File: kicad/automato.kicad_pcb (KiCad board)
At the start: 2 copper layers, 106 x 64 mm, 98 parts, among them J1 USB_C_Receptacle, J2 LiPo, J3 Conn_01x07_Male, J4 Screw_Terminal_01x20, J5 USB_C_Receptacle, J8 Micro_SD_Card_Det, M1 eink-module, Q1 Q_NPN_BCE, Q2 Q_NPN_BCE, Q3 DMG3415U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

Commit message: more routing
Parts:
- moved R17 12.1 mm to (84.6, 71.5)
- moved G*** 11.6 mm to (73.5, 77.0)
- moved C10 11.1 mm to (100.5, 83.9), turned to 180 degrees
- moved R6 10.2 mm to (174.0, 66.8), turned to 270 degrees
- moved R1 9.96 mm to (84.6, 75.6), turned to 0 degrees
- moved R3 9.92 mm to (86.6, 80.7), turned to 90 degrees
- moved C1 8.35 mm to (87.5, 73.7)
- moved C2 8.35 mm to (90.0, 73.7)
- moved R2 8.24 mm to (84.6, 77.8), turned to 180 degrees
- moved C7 8.08 mm to (89.6, 83.1), turned to 180 degrees
- moved D5 7.90 mm to (84.6, 73.5), turned to 0 degrees
- moved JP1 7.21 mm to (169.4, 104.2), turned to 0 degrees
- moved Q1 6.26 mm to (96.8, 83.2), turned to 90 degrees
- moved R5 5.42 mm to (95.2, 76.0), turned to 180 degrees
- moved R4 5.34 mm to (93.5, 83.2), turned to 90 degrees
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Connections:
- J4 pad 10: IO33 -> IO16
- J4 pad 11: IO32 -> 3V3
- J4 pad 12: IO27 -> IO15
- J4 pad 13: IO26 -> GND
- J4 pad 14: VBUS -> IO14
- J4 pad 15: 3V3 -> VBUS
- J4 pad 16: 3V3 -> IO13
- J4 pad 5: GND -> A7
- J4 pad 6: A7 -> A6
- J4 pad 7: A6 -> A1
- J4 pad 8: A1 -> A0
- J4 pad 9: A0 -> 3V3
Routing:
- net VBUS: track 0.00 -> 90.8 mm, vias 0 -> 4
- net EN: track 0.00 -> 80.4 mm, vias 0 -> 4
- net RX: track 0.00 -> 41.6 mm, vias 0 -> 2
- net TX: track 0.00 -> 40.6 mm, vias 0 -> 2
- net RST_LORA: track 0.00 -> 35.4 mm
- net IRQ_LORA: track 0.00 -> 28.5 mm
- net VIN: track 0.00 -> 28.4 mm
- net SPI_CLK: track 0.00 -> 26.5 mm
- net SPI_MISO: track 0.00 -> 26.4 mm
- net CS_LORA: track 0.00 -> 26.3 mm
- net VBAT: track 0.00 -> 26.0 mm, vias 0 -> 2
- net Net-(C3-Pad1): track 0.00 -> 24.6 mm
- net Net-(J3-Pad2): track 0.00 -> 24.1 mm, vias 0 -> 1
- net SPI_MOSI: track 0.00 -> 23.4 mm
- net A0: track 0.00 -> 23.2 mm
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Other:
- net class Default: via_dia 0.8 -> 0.7; via_drill 0.4 -> 0.3

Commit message: add sma
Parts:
- moved TP1 35.4 mm to (153.6, 44.0)
- moved TP2 35.4 mm to (153.6, 47.0)
- moved TP3 35.4 mm to (153.6, 50.0)
- moved TP4 35.4 mm to (153.6, 53.0)
- moved R6 0.73 mm to (173.4, 67.2)
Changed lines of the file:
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@@
   )
   (module Resistor_SMD:R_0805_2012Metric (layer F.Cu)
-    (at 174 66.8 270)
+    (at 173.4 67.2125 270)
     (descr "Resistor SMD 0805 (2012 Metric), square (rectangular) end terminal, IPC_7351 nominal, (Body size source: IPC-SM-782 page 72, https://www.pcb-3d.com/wordpress/wp-content/uploads/ipc-sm-782a_amendment_1_and_2.pdf), generated with kicad-footprint-generator")
     (tags resistor)
@@
   )
   (module TestPoint:TestPoint_Pad_D2.0mm (layer F.Cu)
-    (at 180.25 67.25)
+    (at 153.55 43.95)
     (descr "SMD pad as test Point, diameter 2.0mm")
     (tags "test point SMD pad")
@@
   )
   (module TestPoint:TestPoint_Pad_D2.0mm (layer F.Cu)
-    (at 180.25 70.25)
+    (at 153.55 46.95)
     (descr "SMD pad as test Point, diameter 2.0mm")
     (tags "test point SMD pad")
@@
   )
   (module TestPoint:TestPoint_Pad_D2.0mm (layer F.Cu)
-    (at 180.25 73.25)
+    (at 153.55 49.95)
     (descr "SMD pad as test Point, diameter 2.0mm")
     (tags "test point SMD pad")
@@
   )
   (module TestPoint:TestPoint_Pad_D2.0mm (layer F.Cu)
-    (at 180.25 76.25)
+    (at 153.55 52.95)
     (descr "SMD pad as test Point, diameter 2.0mm")
     (tags "test point SMD pad")

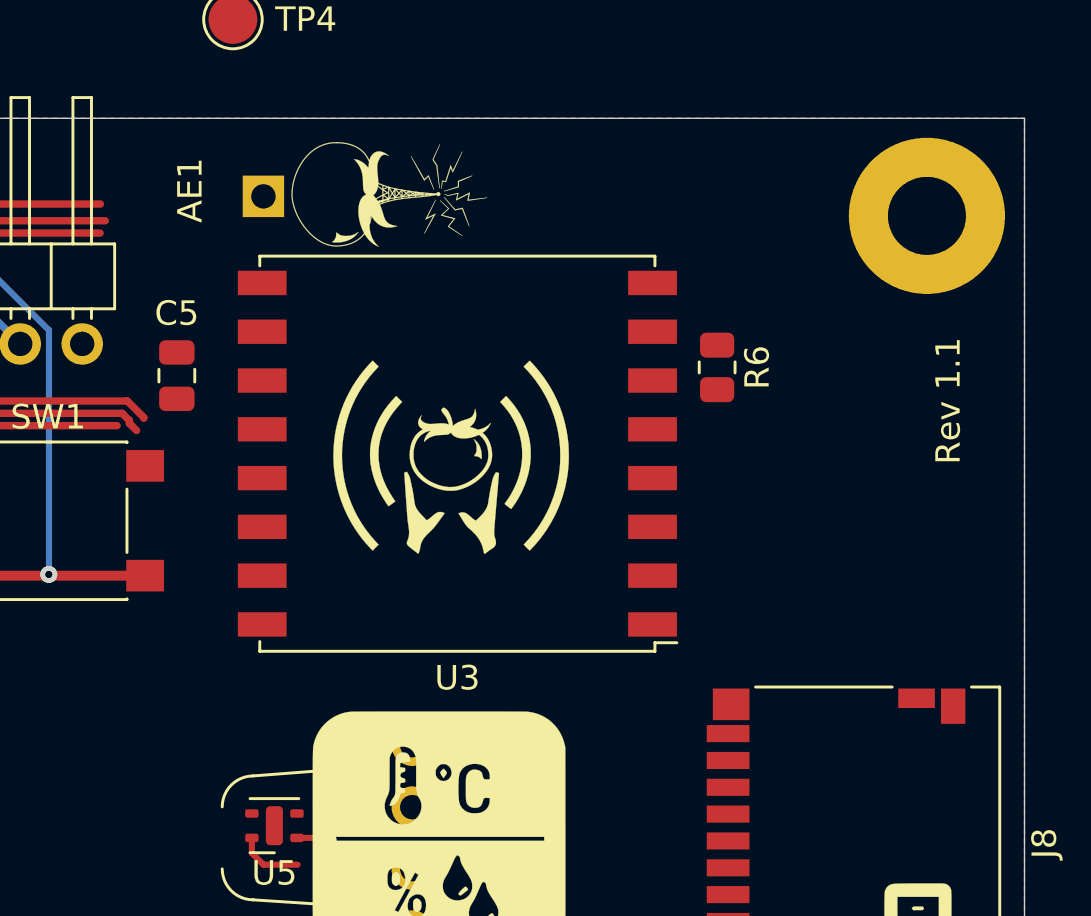
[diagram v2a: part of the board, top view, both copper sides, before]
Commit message: reposition lora
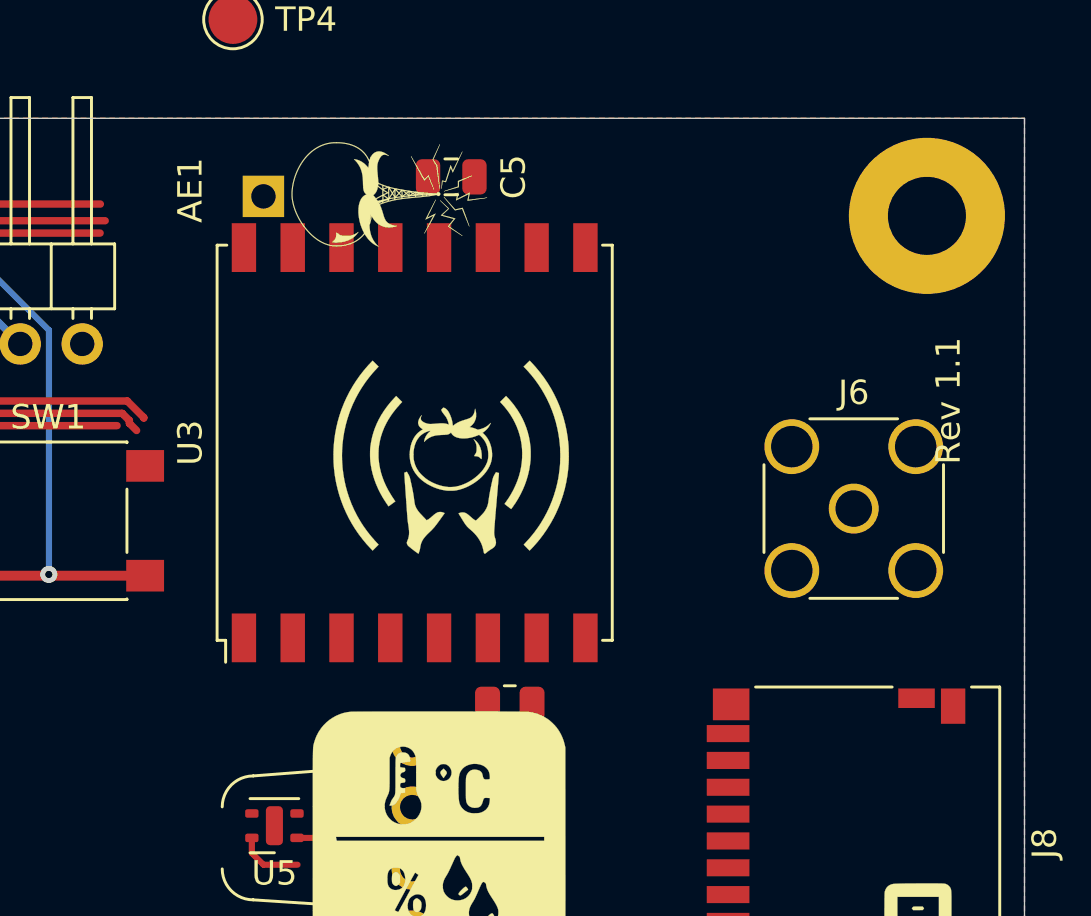
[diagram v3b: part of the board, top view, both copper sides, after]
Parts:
- added J6: Conn_Coaxial, Connector_Coaxial:SMA_Wurth_60312002114503_Vertical, F.Cu at (179.0, 73.0)
- moved R6 16.2 mm to (164.9, 81.0), turned to 180 degrees
- moved C5 13.9 mm to (162.5, 59.4), turned to 0 degrees
- moved U3 1.81 mm to (161.0, 70.3), turned to 90 degrees
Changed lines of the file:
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@@
     (tracks 430)
     (zones 0)
-    (modules 98)
+    (modules 99)
     (nets 116)
   )
@@
     (add_net VIN)
   )
+  (module Connector_Coaxial:SMA_Wurth_60312002114503_Vertical (layer F.Cu)
+    (at 179 73)
+    (descr https://www.we-online.de/katalog/datasheet/60312002114503.pdf)
+    (tags "SMA THT Female Jack Vertical ExtendedLegs")
+    (fp_text reference J6 (at 0 -4.75) (layer F.SilkS)
+      (effects (font (size 1 1) (thickness 0.15)))
+    )
+    (fp_text value Conn_Coaxial (at 0 5) (layer F.Fab)
+      (effects (font (size 1 1) (thickness 0.15)))
+    )
+    (fp_text user %R (at 0 0) (layer F.Fab)
+      (effects (font (size 1 1) (thickness 0.15)))
+    )
+    (fp_circle (center 0 0) (end 3.175 0) (layer F.Fab) (width 0.1))
+    (fp_line (start 4.17 4.17) (end -4.17 4.17) (layer F.CrtYd) (width 0.05))
+    (fp_line (start 4.17 4.17) (end 4.17 -4.17) (layer F.CrtYd) (width 0.05))
+    (fp_line (start -4.17 -4.17) (end -4.17 4.17) (layer F.CrtYd) (width 0.05))
+    (fp_line (start -4.17 -4.17) (end 4.17 -4.17) (layer F.CrtYd) (width 0.05))
+    (fp_line (start -3.5 -3.5) (end 3.5 -3.5) (layer F.Fab) (width 0.1))
+    (fp_line (start -3.5 -3.5) (end -3.5 3.5) (layer F.Fab) (width 0.1))
+    (fp_line (start -3.5 3.5) (end 3.5 3.5) (layer F.Fab) (width 0.1))
+    (fp_line (start 3.5 -3.5) (end 3.5 3.5) (layer F.Fab) (width 0.1))
+    (fp_line (start -3.68 -1.8) (end -3.68 1.8) (layer F.SilkS) (width 0.12))
+    (fp_line (start 3.68 -1.8) (end 3.68 1.8) (layer F.SilkS) (width 0.12))
+    (fp_line (start -1.8 3.68) (end 1.8 3.68) (layer F.SilkS) (width 0.12))
+    (fp_line (start -1.8 -3.68) (end 1.8 -3.68) (layer F.SilkS) (width 0.12))
+    (pad 2 thru_hole circle (at -2.54 2.54) (size 2.25 2.25) (drill 1.7) (layers *.Cu *.Mask)
+      (net 2 GND))
+    (pad 2 thru_hole circle (at -2.54 -2.54) (size 2.25 2.25) (drill 1.7) (layers *.Cu *.Mask)
+      (net 2 GND))
+    (pad 2 thru_hole circle (at 2.54 -2.54) (size 2.25 2.25) (drill 1.7) (layers *.Cu *.Mask)
+      (net 2 GND))
+    (pad 2 thru_hole circle (at 2.54 2.54) (size 2.25 2.25) (drill 1.7) (layers *.Cu *.Mask)
+      (net 2 GND))
+    (pad 1 thru_hole circle (at 0 0) (size 2.05 2.05) (drill 1.5) (layers *.Cu *.Mask)
+      (net 1 "Net-(AE1-Pad1)"))
+    (model ${KISYS3DMOD}/Connector_Coaxial.3dshapes/SMA_Wurth_60312002114503_Vertical.wrl
+      (at (xyz 0 0 0))
+      (scale (xyz 1 1 1))
+      (rotate (xyz 0 0 0))
+    )
+  )
   (module RF_Module:ESP32-WROOM-32 (layer F.Cu)
     (at 116.25 67.5)
@@
   )
   (module RF_Module:HOPERF_RFM9XW_SMD (layer F.Cu)
-    (at 162.75 70.75 180)
+    (at 161 70.3 90)
     (descr "Low Power Long Range Transceiver Module SMD-16 (https://www.hoperf.com/data/upload/portal/20181127/5bfcbea20e9ef.pdf)")
     (tags "LoRa Low Power Long Range Transceiver Module")
     (attr smd)
-    (fp_text reference U3 (at 0 -9.2) (layer F.SilkS)
+    (fp_text reference U3 (at 0 -9.2 90) (layer F.SilkS)
       (effects (font (size 1 1) (thickness 0.15)))
     )
-    (fp_text value RFM95W-915S2 (at 0 9.5) (layer F.Fab)
+    (fp_text value RFM95W-915S2 (at 0 9.5 90) (layer F.Fab)
       (effects (font (size 1 1) (thickness 0.15)))
     )
@@
     (fp_line (start -8.1 -7.75) (end -9 -7.75) (layer F.SilkS) (width 0.12))
     (fp_line (start -7 -8) (end -8 -7) (layer F.Fab) (width 0.1))
-    (fp_text user %R (at 0 0) (layer F.Fab)
+    (fp_text user %R (at 0 0 90) (layer F.Fab)
       (effects (font (size 1 1) (thickness 0.15)))
     )
-    (pad 16 smd rect (at 8 -7 180) (size 2 1) (layers F.Cu F.Paste F.Mask)
+    (pad 16 smd rect (at 8 -7 90) (size 2 1) (layers F.Cu F.Paste F.Mask)
       (net 78 "Net-(U3-Pad16)"))
-    (pad 15 smd rect (at 8 -5 180) (size 2 1) (layers F.Cu F.Paste F.Mask)
+    (pad 15 smd rect (at 8 -5 90) (size 2 1) (layers F.Cu F.Paste F.Mask)
       (net 79 "Net-(U3-Pad15)"))
-    (pad 14 smd rect (at 8 -3 180) (size 2 1) (layers F.Cu F.Paste F.Mask)
+    (pad 14 smd rect (at 8 -3 90) (size 2 1) (layers F.Cu F.Paste F.Mask)
       (net 52 IRQ_LORA))
-    (pad 13 smd rect (at 8 -1 180) (size 2 1) (layers F.Cu F.Paste F.Mask)
+    (pad 13 smd rect (at 8 -1 90) (size 2 1) (layers F.Cu F.Paste F.Mask)
       (net 3 3V3))
-    (pad 12 smd rect (at 8 1 180) (size 2 1) (layers F.Cu F.Paste F.Mask)
+    (pad 12 smd rect (at 8 1 90) (size 2 1) (layers F.Cu F.Paste F.Mask)
       (net 80 "Net-(U3-Pad12)"))
-    (pad 11 smd rect (at 8 3 180) (size 2 1) (layers F.Cu F.Paste F.Mask)
+    (pad 11 smd rect (at 8 3 90) (size 2 1) (layers F.Cu F.Paste F.Mask)
       (net 81 "Net-(U3-Pad11)"))
-    (pad 10 smd rect (at 8 5 180) (size 2 1) (layers F.Cu F.Paste F.Mask)
+    (pad 10 smd rect (at 8 5 90) (size 2 1) (layers F.Cu F.Paste F.Mask)
       (net 2 GND))
-    (pad 9 smd rect (at 8 7 180) (size 2 1) (layers F.Cu F.Paste F.Mask)
+    (pad 9 smd rect (at 8 7 90) (size 2 1) (layers F.Cu F.Paste F.Mask)
       (net 1 "Net-(AE1-Pad1)"))
-    (pad 8 smd rect (at -8 7 180) (size 2 1) (layers F.Cu F.Paste F.Mask)
+    (pad 8 smd rect (at -8 7 90) (size 2 1) (layers F.Cu F.Paste F.Mask)
       (net 2 GND))
-    (pad 7 smd rect (at -8 5 180) (size 2 1) (layers F.Cu F.Paste F.Mask)
+    (pad 7 smd rect (at -8 5 90) (size 2 1) (layers F.Cu F.Paste F.Mask)
       (net 82 "Net-(U3-Pad7)"))
-    (pad 6 smd rect (at -8 3 180) (size 2 1) (layers F.Cu F.Paste F.Mask)
+    (pad 6 smd rect (at -8 3 90) (size 2 1) (layers F.Cu F.Paste F.Mask)
       (net 48 RST_LORA))
-    (pad 5 smd rect (at -8 1 180) (size 2 1) (layers F.Cu F.Paste F.Mask)
+    (pad 5 smd rect (at -8 1 90) (size 2 1) (layers F.Cu F.Paste F.Mask)
       (net 53 CS_LORA))
-    (pad 4 smd rect (at -8 -1 180) (size 2 1) (layers F.Cu F.Paste F.Mask)
+    (pad 4 smd rect (at -8 -1 90) (size 2 1) (layers F.Cu F.Paste F.Mask)
       (net 40 SPI_CLK))
-    (pad 3 smd rect (at -8 -3 180) (size 2 1) (layers F.Cu F.Paste F.Mask)
+    (pad 3 smd rect (at -8 -3 90) (size 2 1) (layers F.Cu F.Paste F.Mask)
       (net 37 SPI_MOSI))
-    (pad 2 smd rect (at -8 -5 180) (size 2 1) (layers F.Cu F.Paste F.Mask)
+    (pad 2 smd rect (at -8 -5 90) (size 2 1) (layers F.Cu F.Paste F.Mask)
       (net 38 SPI_MISO))
-    (pad 1 smd rect (at -8 -7 180) (size 2 1) (layers F.Cu F.Paste F.Mask)
+    (pad 1 smd rect (at -8 -7 90) (size 2 1) (layers F.Cu F.Paste F.Mask)
       (net 2 GND))
     (model ${KISYS3DMOD}/RF_Module.3dshapes/HOPERF_RFM9XW_SMD.wrl
@@
   )
   (module Resistor_SMD:R_0805_2012Metric (layer F.Cu)
-    (at 173.4 67.2125 270)
+    (at 164.9 81 180)
     (descr "Resistor SMD 0805 (2012 Metric), square (rectangular) end terminal, IPC_7351 nominal, (Body size source: IPC-SM-782 page 72, https://www.pcb-3d.com/wordpress/wp-content/uploads/ipc-sm-782a_amendment_1_and_2.pdf), generated with kicad-footprint-generator")
     (tags resistor)
     (attr smd)
-    (fp_text reference R6 (at 0 -1.65 90) (layer F.SilkS)
+    (fp_text reference R6 (at 0 -1.65) (layer F.SilkS)
       (effects (font (size 1 1) (thickness 0.15)))
     )
-    (fp_text value 100k (at 0 1.65 90) (layer F.Fab)
+    (fp_text value 100k (at 0 1.65) (layer F.Fab)
       (effects (font (size 1 1) (thickness 0.15)))
     )
@@
     (fp_line (start 1.68 -0.95) (end 1.68 0.95) (layer F.CrtYd) (width 0.05))
     (fp_line (start 1.68 0.95) (end -1.68 0.95) (layer F.CrtYd) (width 0.05))
-    (fp_text user %R (at 0 0 90) (layer F.Fab)
+    (fp_text user %R (at 0 0) (layer F.Fab)
       (effects (font (size 0.5 0.5) (thickness 0.08)))
     )
-    (pad 2 smd roundrect (at 0.9125 0 270) (size 1.025 1.4) (layers F.Cu F.Paste F.Mask) (roundrect_rratio 0.243902)
+    (pad 2 smd roundrect (at 0.9125 0 180) (size 1.025 1.4) (layers F.Cu F.Paste F.Mask) (roundrect_rratio 0.243902)
       (net 48 RST_LORA))
-    (pad 1 smd roundrect (at -0.9125 0 270) (size 1.025 1.4) (layers F.Cu F.Paste F.Mask) (roundrect_rratio 0.243902)
+    (pad 1 smd roundrect (at -0.9125 0 180) (size 1.025 1.4) (layers F.Cu F.Paste F.Mask) (roundrect_rratio 0.243902)
       (net 3 3V3))
     (model ${KISYS3DMOD}/Resistor_SMD.3dshapes/R_0805_2012Metric.wrl
@@
   )
   (module Capacitor_SMD:C_0805_2012Metric (layer F.Cu)
-    (at 151.25 67.55 90)
+    (at 162.5 59.4)
     (descr "Capacitor SMD 0805 (2012 Metric), square (rectangular) end terminal, IPC_7351 nominal, (Body size source: IPC-SM-782 page 76, https://www.pcb-3d.com/wordpress/wp-content/uploads/ipc-sm-782a_amendment_1_and_2.pdf, https://docs.google.com/spreadsheets/d/1BsfQQcO9C6DZCsRaXUlFlo91Tg2WpOkGARC1WS5S8t0/edit?usp=sharing), generated with kicad-footprint-generator")
     (tags capacitor)
     (attr smd)
-    (fp_text reference C5 (at 2.55 0 180) (layer F.SilkS)
+    (fp_text reference C5 (at 2.55 0 270) (layer F.SilkS)
       (effects (font (size 1 1) (thickness 0.15)))
     )
-    (fp_text value "10 uF" (at 0 1.68 90) (layer F.Fab)
+    (fp_text value "10 uF" (at 0 1.68) (layer F.Fab)
       (effects (font (size 1 1) (thickness 0.15)))
     )
@@
     (fp_line (start 1.7 -0.98) (end 1.7 0.98) (layer F.CrtYd) (width 0.05))
     (fp_line (start 1.7 0.98) (end -1.7 0.98) (layer F.CrtYd) (width 0.05))
-    (fp_text user %R (at 0 0 90) (layer F.Fab)
+    (fp_text user %R (at 0 0) (layer F.Fab)
       (effects (font (size 0.5 0.5) (thickness 0.08)))
     )
-    (pad 2 smd roundrect (at 0.95 0 90) (size 1 1.45) (layers F.Cu F.Paste F.Mask) (roundrect_rratio 0.25)
+    (pad 2 smd roundrect (at 0.95 0) (size 1 1.45) (layers F.Cu F.Paste F.Mask) (roundrect_rratio 0.25)
       (net 2 GND))
-    (pad 1 smd roundrect (at -0.95 0 90) (size 1 1.45) (layers F.Cu F.Paste F.Mask) (roundrect_rratio 0.25)
+    (pad 1 smd roundrect (at -0.95 0) (size 1 1.45) (layers F.Cu F.Paste F.Mask) (roundrect_rratio 0.25)
       (net 3 3V3))
     (model ${KISYS3DMOD}/Capacitor_SMD.3dshapes/C_0805_2012Metric.wrl

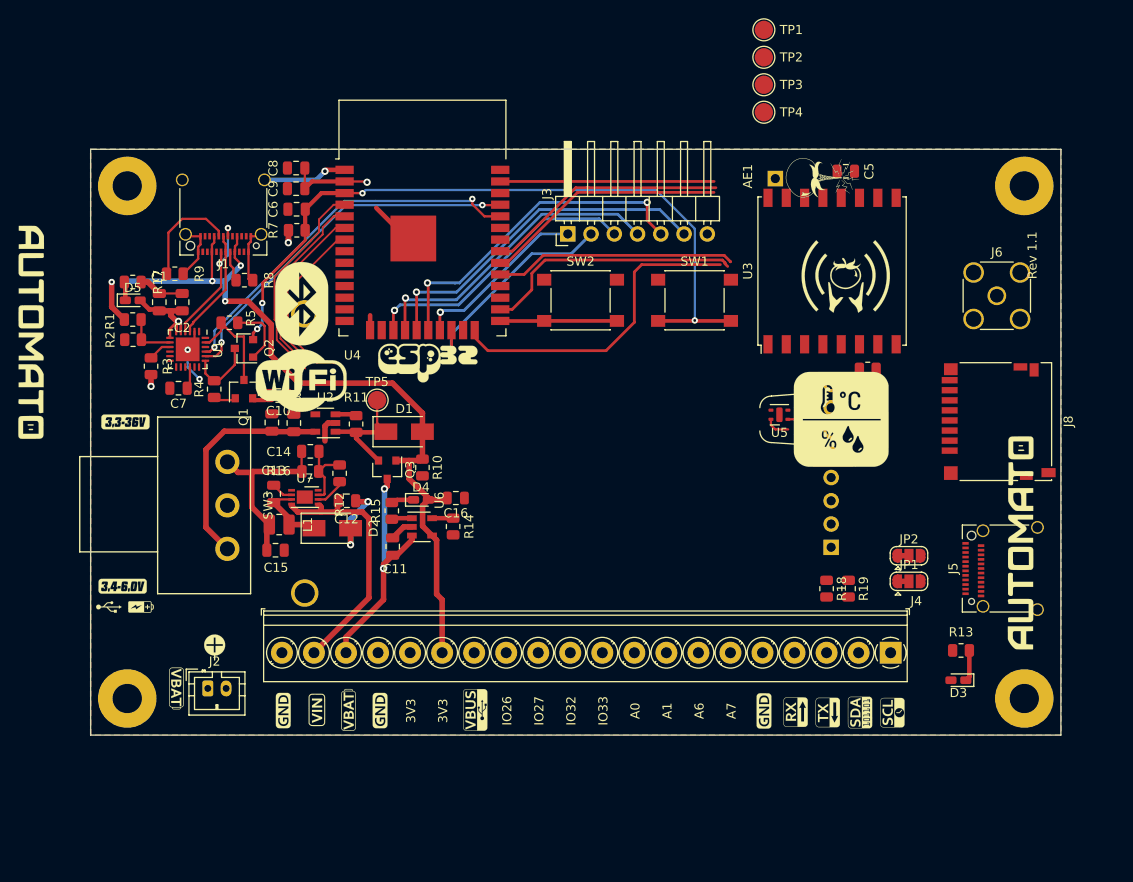
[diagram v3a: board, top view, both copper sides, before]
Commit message: moved indicator led
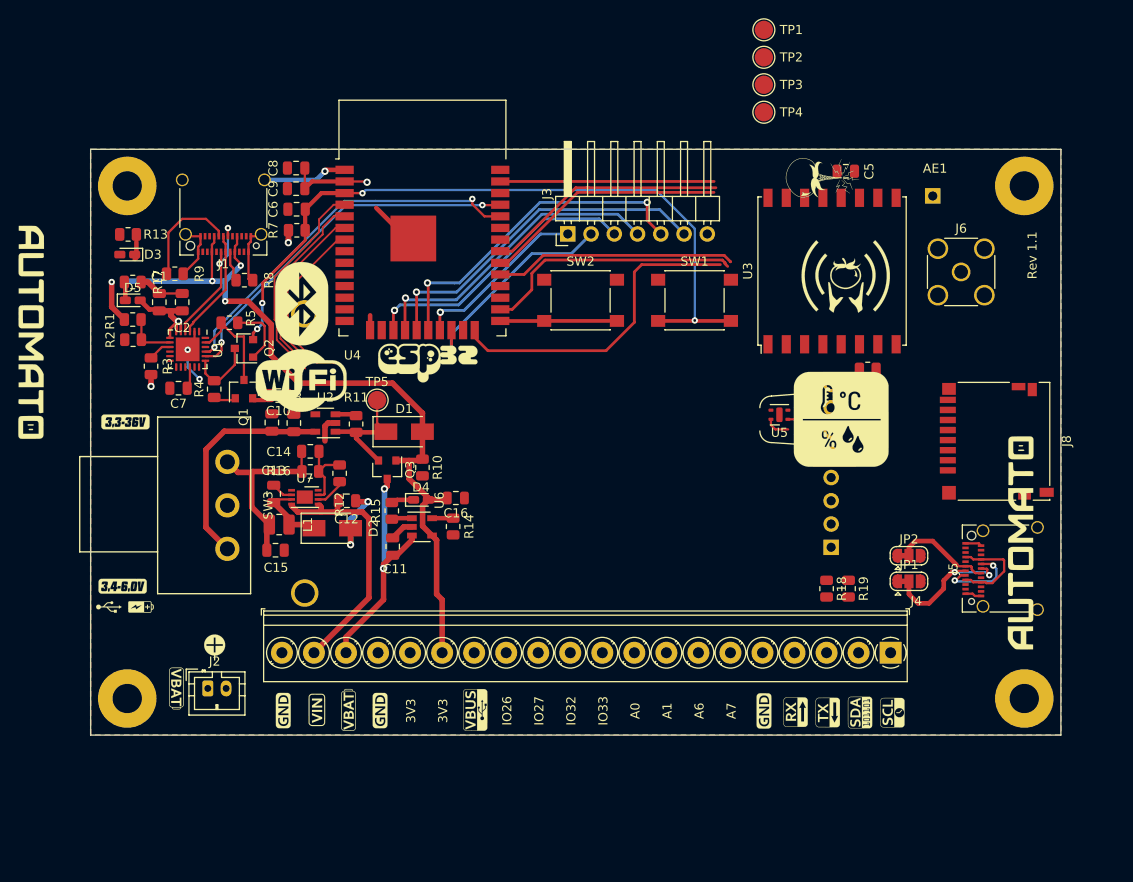
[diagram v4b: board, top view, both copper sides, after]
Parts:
- moved D3 102.0 mm to (84.0, 68.5)
- moved R13 101.7 mm to (84.1, 66.3)
- moved AE1 17.3 mm to (172.0, 62.1), turned to 270 degrees
- moved J6 4.69 mm to (175.1, 70.4)
- moved J8 2.16 mm to (179.0, 88.9)
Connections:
- net IRQ_TCH renamed U2_TXD
- net LED_LCD renamed U2_RXD
- U4 pad 14: Net-(U4-Pad14) -> CS_SD
- U4 pad 28: CS_SD -> CS_RELAY
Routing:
- net Net-(J5-PadA6): track 0.00 -> 15.4 mm, vias 0 -> 2
- net VBUS: track 90.8 -> 101.3 mm
- net Net-(J5-PadA7): track 0.00 -> 10.4 mm
- net CS_RELAY: track 0.00 -> 9.00 mm, vias 0 -> 2
- net GND: track 60.3 -> 63.9 mm
- net Net-(D3-Pad1): track 4.05 -> 1.98 mm
